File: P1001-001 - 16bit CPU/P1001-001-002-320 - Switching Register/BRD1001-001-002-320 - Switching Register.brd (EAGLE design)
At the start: 200 x 48 mm, 26 parts, among them IC1 74HC173D, IC10 74LS32D, IC12 74AC245DW, IC2 74HC173D, IC27 MEGA8535-A, IC3 74HC173D, IC4 74HC173D, IC5 74ALS21D, IC6 74ALS21D, IC7 74AC245DW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

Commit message: Finished All Boards
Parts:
- added C1, C2, C3, C4: 1uF, rcl:C1206
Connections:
- net GND: now also C1.2, C2.2, C3.2, C4.2
- net VCC: now also C1.1, C2.1, C3.1, C4.1
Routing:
- net VCC: track 406.2 -> 491.0 mm, vias 24 -> 27
- net GND: track 444.8 -> 525.6 mm, vias 29 -> 35

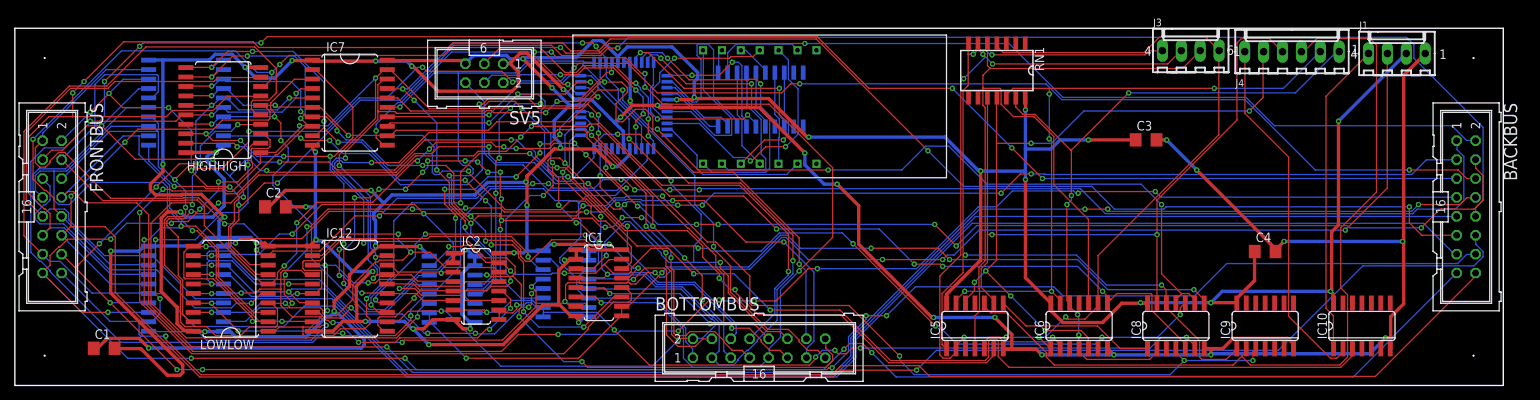
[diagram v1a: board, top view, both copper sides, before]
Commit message: Fix problems with registers
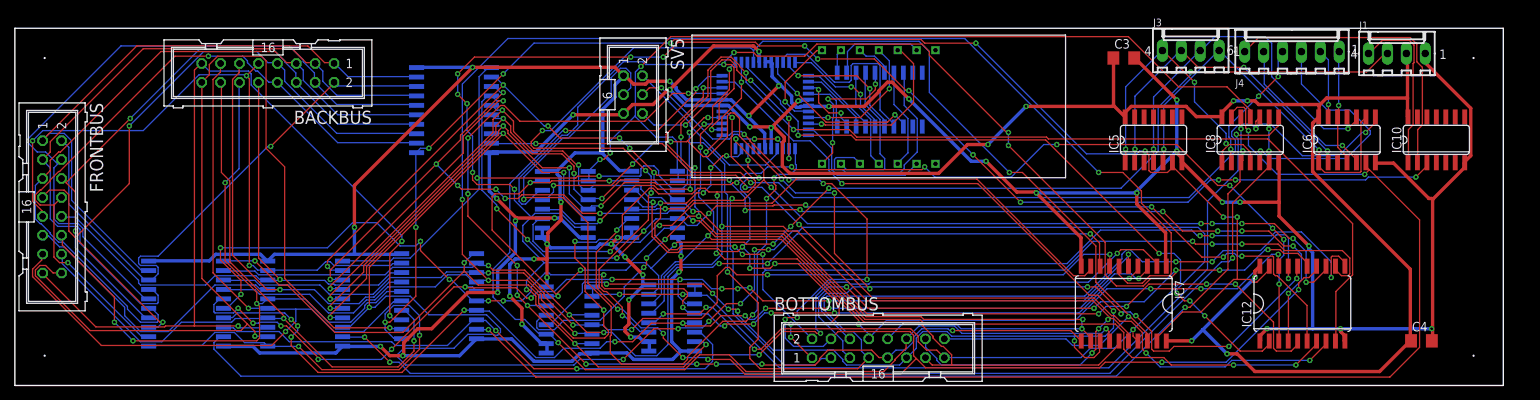
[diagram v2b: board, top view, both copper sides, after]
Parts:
- removed C1, C2: 1uF, rcl:C1206
- removed IC9: 74ALS08D, 74xx-us:SO14
- removed RN1: (no value), resistor-dil:SOMC14
- moved BACKBUS 162.0 mm to (34.0, 42.0), turned to 180 degrees
- moved IC12 128.0 mm to (173.0, 11.0), turned to 0 degrees
- moved IC7 107.4 mm to (149.0, 11.0), turned to 180 degrees
- moved IC6 43.8 mm to (179.0, 33.0)
- moved LOWLOW 38.4 mm to (59.0, 37.0), flipped to the bottom
- moved HIGHHIGH 38.3 mm to (57.0, 12.0), flipped to the bottom
- moved IC5 34.7 mm to (153.0, 33.0)
- moved IC4 29.8 mm to (88.2, 9.07), turned to 90 degrees
- moved LOWHIGH 27.0 mm to (23.0, 11.0)
- moved IC10 26.9 mm to (191.0, 33.0)
- moved IC8 26.9 mm to (166.0, 33.0)
- moved C4 24.2 mm to (189.0, 6.00)
- moved SV5 20.2 mm to (83.0, 39.1), turned to 270 degrees
- moved IC27 19.0 mm to (100.8, 37.6)
- moved IC2 16.3 mm to (74.0, 24.3), flipped to the bottom, turned to 90 degrees
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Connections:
- removed net !IN_CLEAR: RN1.9
- removed net !REG_IN: IC8.3
- removed net N$1: IC5.8, IC8.1
- removed net N$23: RN1.8
- net !HIGH_HIGH: now also IC8.13; no longer IC8.10
- net !HIGH_LOW: now also IC8.6, IC8.9; no longer IC8.4, IC9.3
- net !IN: no longer IC8.2, RN1.13
- net !IN_HIGH_HIGH: no longer IC5.12, RN1.11
- net !IN_HIGH_LOW: now also IC8.5; no longer IC5.10, IC9.2
- net !IN_LOW_HIGH: now also IC8.2; no longer IC5.9, IC8.13, RN1.10
- net !IN_LOW_LOW: no longer IC5.13, RN1.12
- net !LOW_HIGH: now also IC8.12, IC8.3; no longer IC8.11, IC8.9
- net !LOW_LOW: now also IC8.10; no longer IC8.5
- net !OUT: no longer RN1.4
- net !OUT_HIGH: no longer RN1.6
- net !OUT_LOW: no longer RN1.5
- net !OUT_SWAP: now also IC8.1, IC8.4; no longer IC8.12, IC9.1, RN1.7
- net !REG_IN_LOW: now also IC8.11; no longer IC8.6
- net GND: no longer C1.2, C2.2, IC9.7
- net VCC: no longer C1.1, C2.1, IC9.14, RN1.14
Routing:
- net MAIN_BUS10: track 271.7 -> 93.6 mm, vias 4 -> 1
- net MAIN_BUS5: track 258.6 -> 83.4 mm, vias 8 -> 2
- net MAIN_BUS6: track 269.8 -> 95.2 mm, vias 9 -> 2
- net MAIN_BUS4: track 267.6 -> 93.5 mm, vias 7 -> 0
- net MAIN_BUS7: track 267.1 -> 93.1 mm, vias 5 -> 2
- net BUS7: track 64.2 -> 237.3 mm, vias 4 -> 12
- net MAIN_BUS12: track 277.8 -> 104.7 mm, vias 0 -> 2
- net MAIN_BUS9: track 251.7 -> 79.3 mm, vias 4 -> 1
- net MAIN_BUS11: track 266.4 -> 95.4 mm, vias 3 -> 4
- net MAIN_BUS8: track 257.2 -> 92.8 mm, vias 0 -> 3
- net MAIN_BUS1: track 235.9 -> 77.4 mm, vias 9 -> 1
- net MAIN_BUS3: track 250.1 -> 93.5 mm, vias 14 -> 0
- net MAIN_BUS0: track 238.6 -> 84.3 mm, vias 9 -> 0
- net MAIN_BUS13: track 244.8 -> 99.6 mm, vias 10 -> 2
- net MAIN_BUS14: track 264.2 -> 119.8 mm, vias 9 -> 3
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
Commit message: Check in the first try at soldering up the board
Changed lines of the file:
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@@
 <hole x="4" y="44" drill="0.12"/>
 <hole x="196" y="4" drill="0.12"/>
+<hole x="4" y="44" drill="3"/>
+<hole x="4" y="4" drill="3"/>
+<hole x="196" y="4" drill="3"/>
+<hole x="196" y="44" drill="3"/>
 </plain>
 <attributes>
